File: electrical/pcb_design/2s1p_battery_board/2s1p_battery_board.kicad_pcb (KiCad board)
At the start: 4 copper layers, 77 x 96 mm, 59 parts, among them J1 TE_Connectivity_7-5530843-7, J10 TE_Connectivity_7-5530843-7, J11 TE_Connectivity_7-5530843-7, J12 TE_Connectivity_7-5530843-7, J13 TE_Connectivity_7-5530843-7, J14 TE_Connectivity_7-5530843-7, J15 TE_Connectivity_7-5530843-7, J16 TE_Connectivity_7-5530843-7, J17 STLINK_TagConnect_6, J2 TE_Connectivity_7-5530843-7, J3 TE_Connectivity_7-5530843-7, J4 TE_Connectivity_7-5530843-7, J5 TE_Connectivity_7-5530843-7, J6 TE_Connectivity_7-5530843-7, J7 TE_Connectivity_7-5530843-7, J8 TE_Connectivity_7-5530843-7, J9 TE_Connectivity_7-5530843-7, U1 BMI323, U2 BMI323, U3 TCAN330, U4 STM32L452CEU6, U5 TCAN330

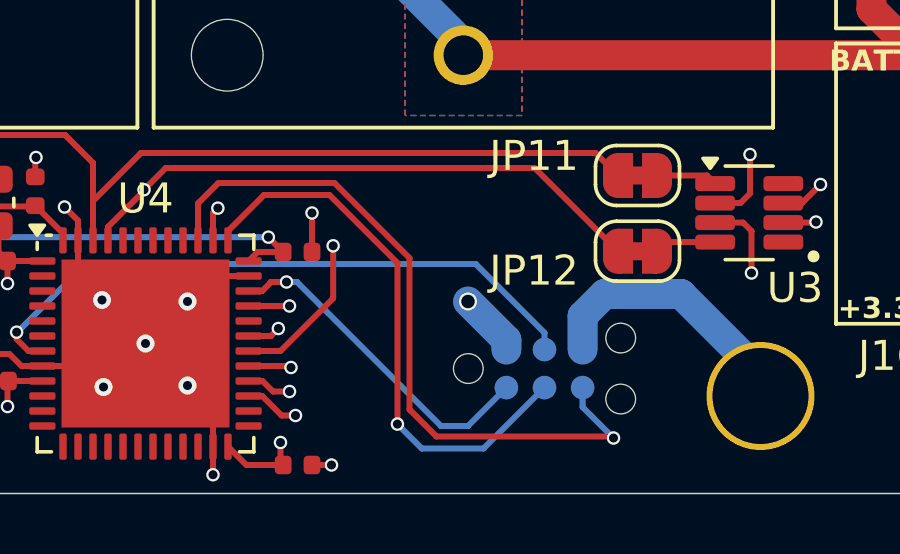
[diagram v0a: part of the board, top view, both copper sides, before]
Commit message: Verified schematics and PCBs for all boards
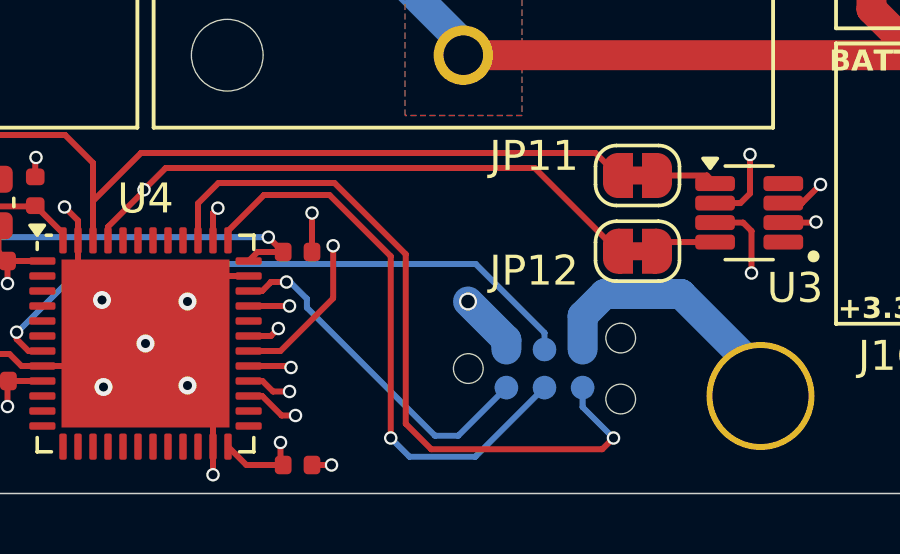
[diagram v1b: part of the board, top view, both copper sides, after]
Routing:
- net TRACESWO: track 23.9 -> 24.6 mm
- net SWCLK: track 18.9 -> 19.5 mm

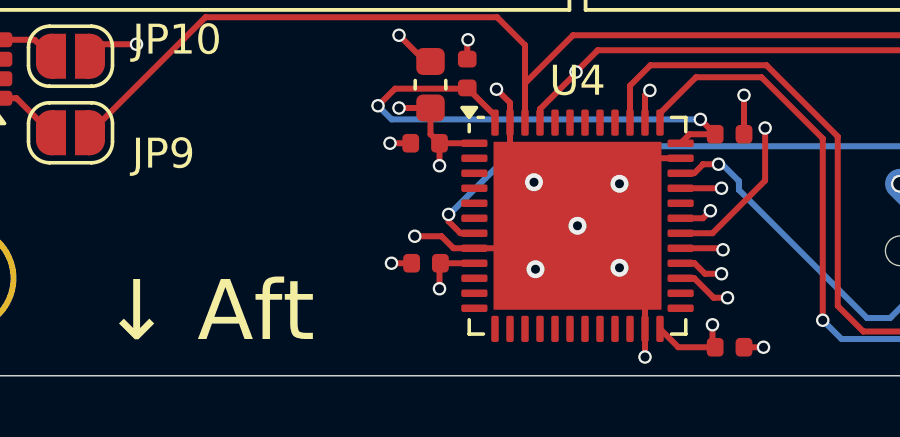
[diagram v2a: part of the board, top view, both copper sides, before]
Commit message: Added board identification mechanism. Updated production files and 3D models.
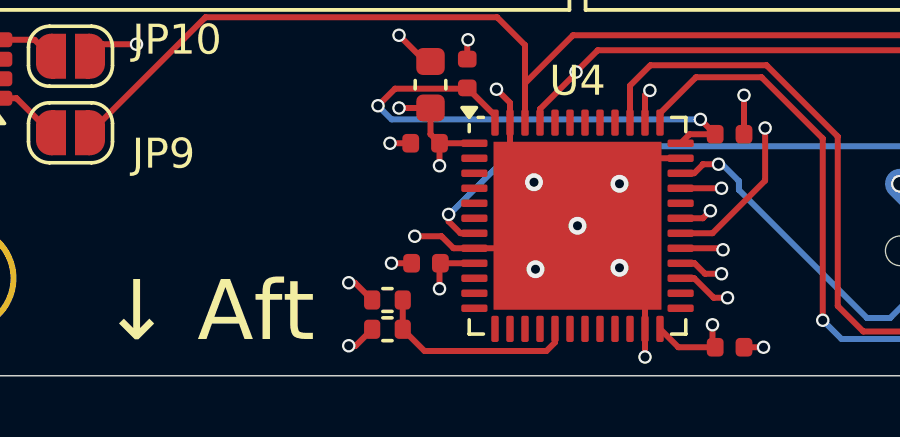
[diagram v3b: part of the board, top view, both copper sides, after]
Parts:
- added R13: 715k, footprints:Nondescript_R_0402_1005Metric, F.Cu at (146.6, 130.8)
- added R8: 301k, footprints:Nondescript_R_0402_1005Metric, F.Cu at (146.6, 131.8)
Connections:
- U4 pad 17: unconnected-(U4-PA7-Pad17) -> BOARD_ID
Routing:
- net BOARD_ID: track 0.00 -> 6.92 mm
- net +3.3V: track 42.5 -> 43.5 mm, vias 18 -> 19
- net GND: track 38.7 -> 39.7 mm, vias 26 -> 27

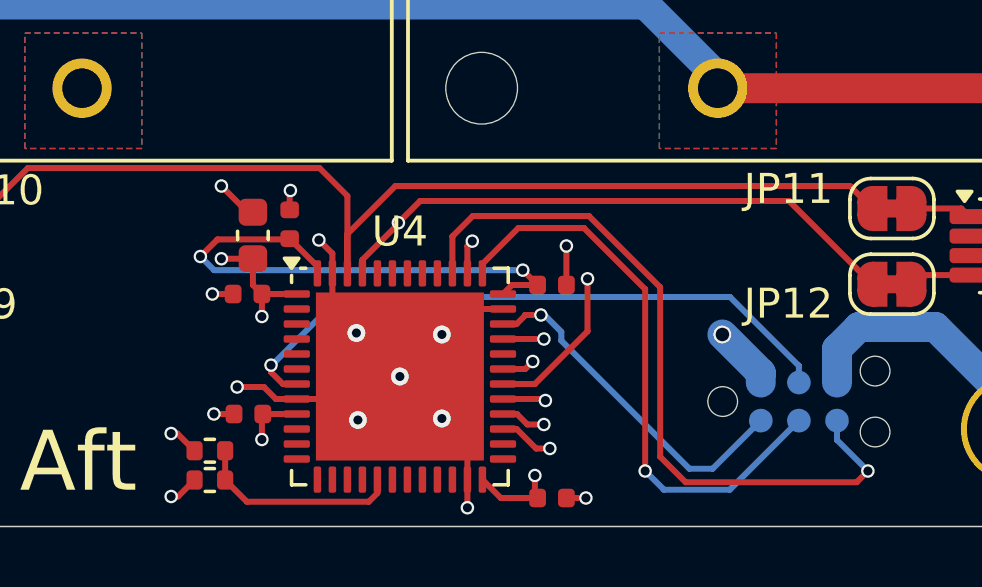
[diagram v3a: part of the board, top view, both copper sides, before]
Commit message: Modified PCB designs to use local footprint for the STM32L452CEU6 part in order to configure the 3D model for this part.
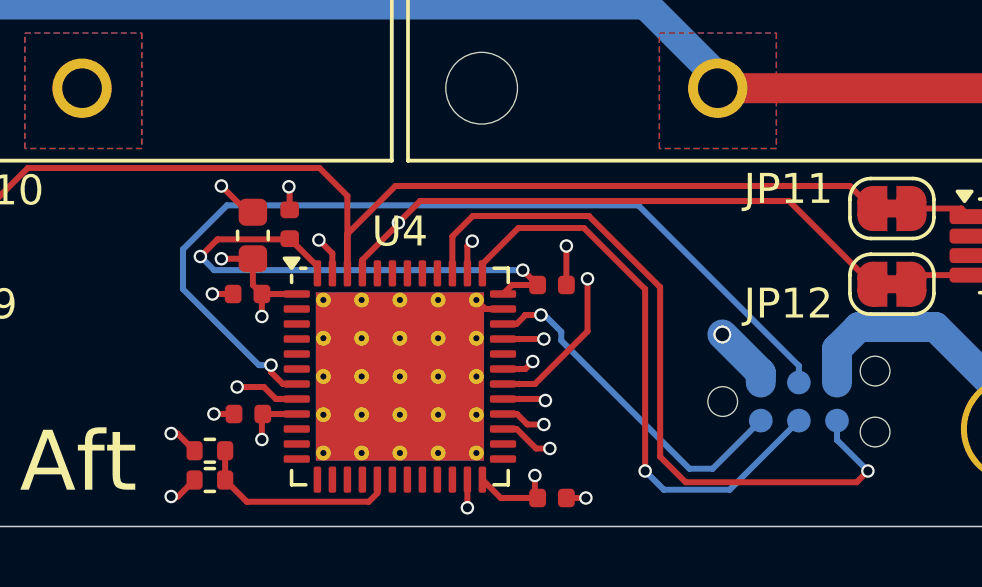
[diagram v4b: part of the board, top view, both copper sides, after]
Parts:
- U4: footprint Package_DFN_QFN:QFN-48-1EP_7x7mm_P0.5mm_EP5.6x5.6mm -> footprints:QFN-48-1EP_7x7mm_P0.5mm_EP5.6x5.6mm_ThermalVias
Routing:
- net NRST: track 21.3 -> 30.5 mm
- net GND: track 39.7 -> 34.7 mm, vias 27 -> 22

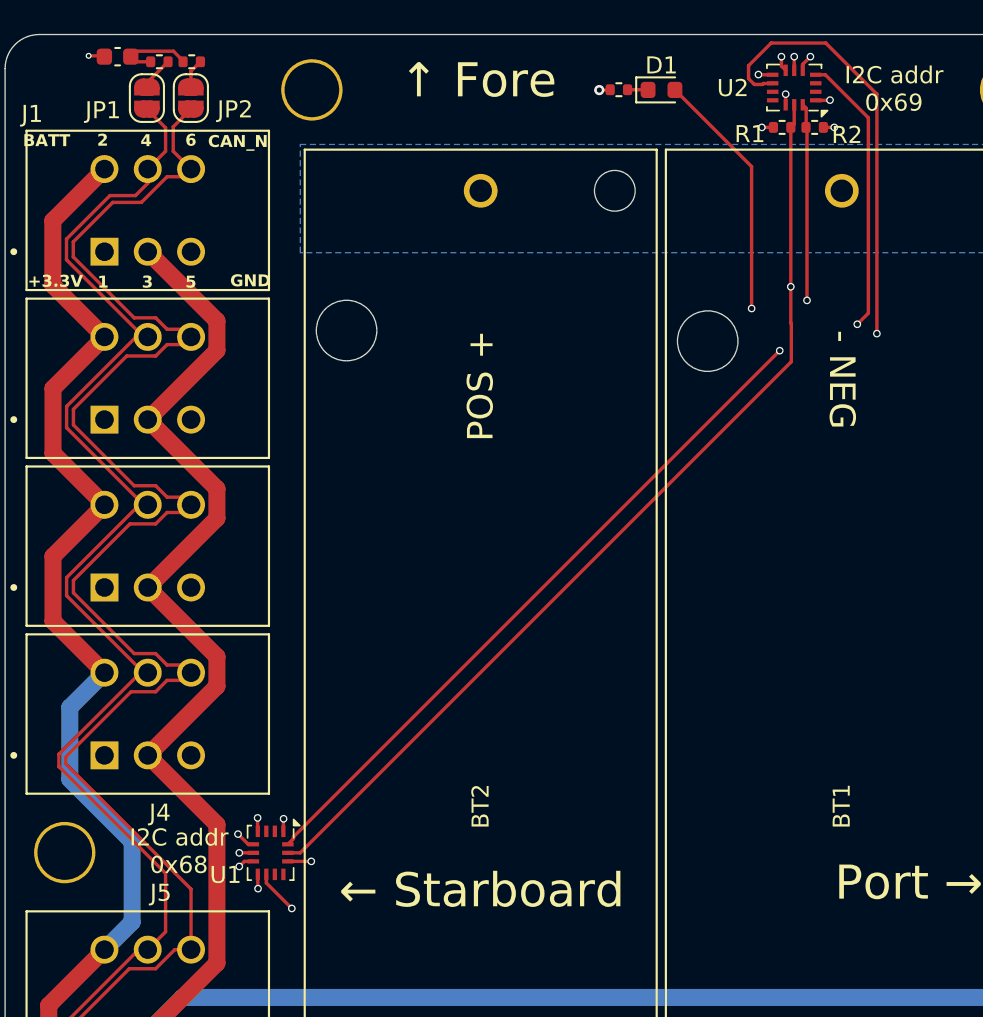
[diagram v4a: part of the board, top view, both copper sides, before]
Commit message: Added decoupling capacitors for IMUs on battery boards
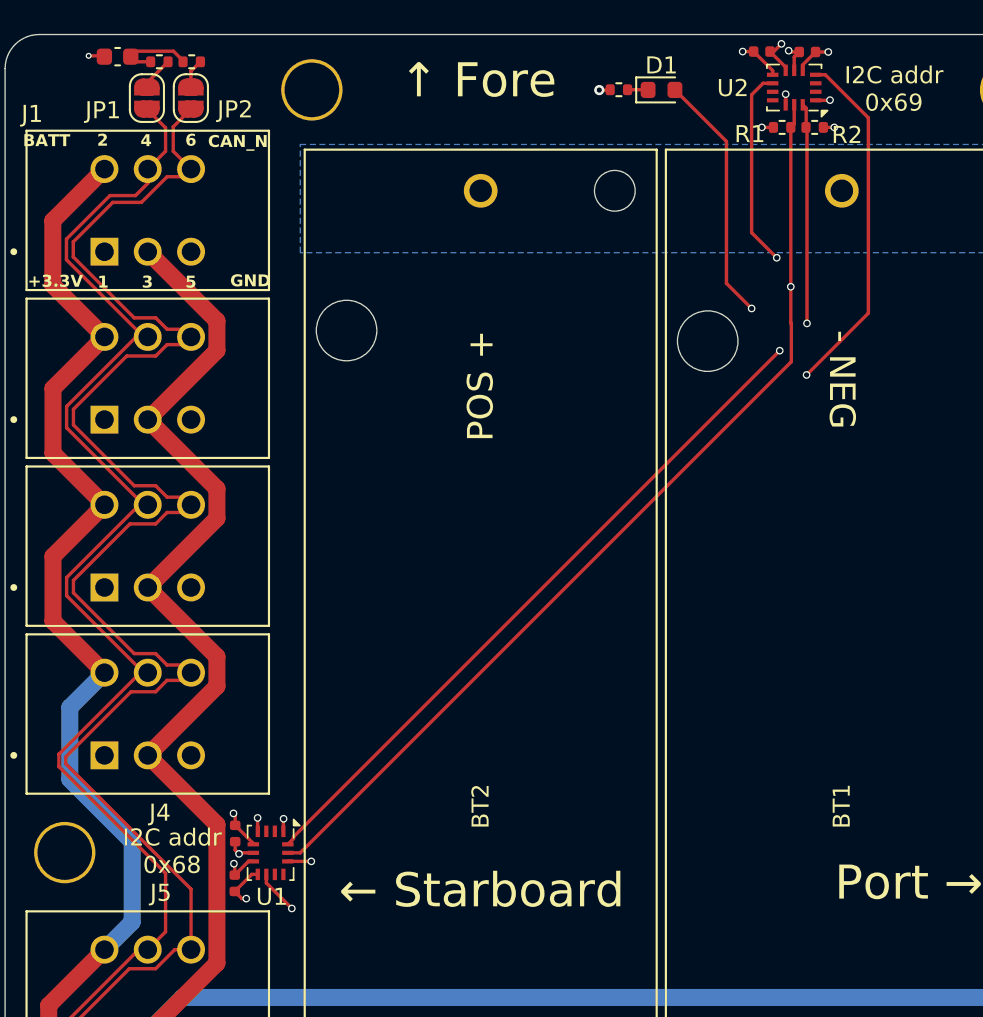
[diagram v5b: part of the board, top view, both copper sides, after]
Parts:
- added C11: 100n, footprints:Nondescript_C_0402_1005Metric, F.Cu at (127.9, 84.2)
- added C12: 100n, footprints:Nondescript_C_0402_1005Metric, F.Cu at (127.9, 87.1)
- added C13: 100n, footprints:Nondescript_C_0402_1005Metric, F.Cu at (161.5, 38.4)
- added C14: 100n, footprints:Nondescript_C_0402_1005Metric, F.Cu at (158.8, 38.3)
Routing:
- net IMU2_INT2: track 106.6 -> 96.5 mm
- net +3.3V: track 43.5 -> 49.2 mm
- net GND: track 34.7 -> 39.2 mm

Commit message: Checkpointing work rearranging backplane pin-out
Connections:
- J1 pad 3: +5V -> GND
- J1 pad 4: CAN_2_P -> unconnected-(J1-Pad4)
- J1 pad 5: GND -> CAN_2_P
- J10 pad 3: +5V -> GND
- J10 pad 4: CAN_P -> unconnected-(J10-Pad4)
- J10 pad 5: GND -> CAN_P
- J11 pad 3: +5V -> GND
- J11 pad 4: CAN_P -> unconnected-(J11-Pad4)
- J11 pad 5: GND -> CAN_P
- J12 pad 3: +5V -> GND
- J12 pad 4: CAN_P -> unconnected-(J12-Pad4)
- J12 pad 5: GND -> CAN_P
- J13 pad 3: +5V -> GND
- J13 pad 4: CAN_P -> unconnected-(J13-Pad4)
- J13 pad 5: GND -> CAN_P
- J14 pad 3: +5V -> GND
- J14 pad 4: CAN_P -> unconnected-(J14-Pad4)
- J14 pad 5: GND -> CAN_P
- J15 pad 3: +5V -> GND
- J15 pad 4: CAN_P -> unconnected-(J15-Pad4)
- J15 pad 5: GND -> CAN_P
- J16 pad 3: +5V -> GND
- J16 pad 4: CAN_P -> unconnected-(J16-Pad4)
- J16 pad 5: GND -> CAN_P
- J2 pad 3: +5V -> GND
- J2 pad 4: CAN_2_P -> unconnected-(J2-Pad4)
- J2 pad 5: GND -> CAN_2_P
- J3 pad 3: +5V -> GND
- J3 pad 4: CAN_2_P -> unconnected-(J3-Pad4)
- J3 pad 5: GND -> CAN_2_P
- J4 pad 3: +5V -> GND
- J4 pad 4: CAN_2_P -> unconnected-(J4-Pad4)
- J4 pad 5: GND -> CAN_2_P
- J5 pad 3: +5V -> GND
- J5 pad 4: CAN_2_P -> unconnected-(J5-Pad4)
- J5 pad 5: GND -> CAN_2_P
- J6 pad 3: +5V -> GND
- J6 pad 4: CAN_2_P -> unconnected-(J6-Pad4)
- J6 pad 5: GND -> CAN_2_P
- J7 pad 3: +5V -> GND
- J7 pad 4: CAN_2_P -> unconnected-(J7-Pad4)
- J7 pad 5: GND -> CAN_2_P
- J8 pad 3: +5V -> GND
- J8 pad 4: CAN_2_P -> unconnected-(J8-Pad4)
- J8 pad 5: GND -> CAN_2_P
- J9 pad 3: +5V -> GND
- J9 pad 4: CAN_P -> unconnected-(J9-Pad4)
- J9 pad 5: GND -> CAN_P
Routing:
- net +5V: track 260.3 -> 0.00 mm
- net CAN_2_N: track 165.0 -> 7.84 mm
- net CAN_N: track 156.9 -> 1.10 mm
- net CAN_2_P: track 136.6 -> 0.00 mm, vias 1 -> 0
- net CAN_P: track 133.1 -> 0.00 mm, vias 1 -> 0
- net GND: track 39.2 -> 100.0 mm
